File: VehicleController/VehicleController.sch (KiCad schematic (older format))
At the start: 58 parts, among them J1 CONN_02X06, J2 USF_SLAVE_I2C, J3 USB_A, J4 USB_A, J5 I2C_0, J6 I2C_1, P1 OUTPUTS, P2 OUTPUTS, Q1 Shutdown_FET, Q2 AIR_FET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

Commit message: Re-do MX120, GDS->GSD, Associations.
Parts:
- removed Q1: Shutdown_FET, TO_SOT_Packages_SMD:SOT-23_Handsoldering, symbol Q_NMOS_GDS
- removed Q2: AIR_FET, TO_SOT_Packages_SMD:SOT-23_Handsoldering, symbol Q_NMOS_GDS
- added Q1, Q2: Q_NMOS_GSD, TO_SOT_Packages_SMD:SOT-23_Handsoldering, symbol Q_NMOS_GSD
- BT1: footprint (none) -> UNCA Motorsports:BATT_CR1220
- D1, D2: footprint (none) -> Diodes_SMD:D_SOD-323_HandSoldering
- F1, F2, F3, F4, F5, F6, F7, F8: footprint (none) -> Resistors_SMD:R_1210_HandSoldering
- J1, P1, P2: footprint (none) -> UNCA Motorsports:MX120G-12
- J2, J5, J6: footprint (none) -> Pin_Headers:Pin_Header_Straight_1x03_Pitch2.54mm
- U1, U2: footprint (none) -> UNCA Motorsports:SOIC20-WIDE
- U3: footprint UNCAMotorsports:TO-252-5 -> UNCA Motorsports:TO-252-5
- U4: footprint (none) -> UNCA Motorsports:TO-252-5
- U5: footprint UNCAMotorsports:LGA-16-3x3 -> UNCA Motorsports:LGA-16-3x3
- U6: footprint UNCAMotorsports:UltimateSensorFusion -> UNCA Motorsports:UltimateSensorFusion
- U7: footprint UNCAMotorsports:Teensy_3.5 -> UNCA Motorsports:Teensy_3.5

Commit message: Library Fixes
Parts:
- BT1: footprint UNCA Motorsports:BATT_CR1220 -> UNCAMotorsports:BATT_CR1220
- D1, D2: footprint Diodes_SMD:D_SOD-323_HandSoldering -> Diodes_SMD:SOD-323
- J1, P1, P2: footprint UNCA Motorsports:MX120G-12 -> UNCAMotorsports:MX120G-12
- J2, J5, J6: footprint Pin_Headers:Pin_Header_Straight_1x03_Pitch2.54mm -> Pin_Headers:Pin_Header_Straight_1x03
- U1, U2: footprint UNCA Motorsports:SOIC20-WIDE -> UNCAMotorsports:SOIC20-WIDE
- U3, U4: footprint UNCA Motorsports:TO-252-5 -> UNCAMotorsports:TO-252-5
- U5: footprint UNCA Motorsports:LGA-16-3x3 -> UNCAMotorsports:LGA-16-3x3
- U6: footprint UNCA Motorsports:UltimateSensorFusion -> UNCAMotorsports:UltimateSensorFusion
- U7: footprint UNCA Motorsports:Teensy_3.5 -> UNCAMotorsports:Teensy_3.5
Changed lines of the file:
@@
 F 0 "BT1" H 6718 3846 50  0000 L CNN
 F 1 "CR1220" H 6718 3755 50  0000 L CNN
-F 2 "UNCA Motorsports:BATT_CR1220" V 6600 3810 50  0001 C CNN
+F 2 "UNCAMotorsports:BATT_CR1220" V 6600 3810 50  0001 C CNN
 F 3 "" V 6600 3810 50  0000 C CNN
 	1    6600 3750
@@
 F 0 "U6" H 10450 9437 60  0000 C CNN
 F 1 "UltimateSensorFusion" H 10450 9331 60  0000 C CNN
-F 2 "UNCA Motorsports:UltimateSensorFusion" H 10450 8850 60  0001 C CNN
+F 2 "UNCAMotorsports:UltimateSensorFusion" H 10450 8850 60  0001 C CNN
 F 3 "" H 10450 8850 60  0001 C CNN
 	1    10450 8950
@@
 F 0 "U3" H 3150 3437 60  0000 C CNN
 F 1 "BTS6133D" H 3150 3331 60  0000 C CNN
-F 2 "UNCA Motorsports:TO-252-5" H 3300 3250 60  0001 C CNN
+F 2 "UNCAMotorsports:TO-252-5" H 3300 3250 60  0001 C CNN
 F 3 "" H 3300 3250 60  0000 C CNN
 	1    3150 3050
@@
 F 0 "U5" H 8700 10037 60  0000 C CNN
 F 1 "H3LIS331DL" H 8700 9931 60  0000 C CNN
-F 2 "UNCA Motorsports:LGA-16-3x3" H 8500 9350 60  0001 C CNN
+F 2 "UNCAMotorsports:LGA-16-3x3" H 8500 9350 60  0001 C CNN
 F 3 "" H 8500 9350 60  0000 C CNN
 	1    8700 9250
@@
 F 0 "U4" H 2950 5200 60  0000 C CNN
 F 1 "BTS6133D" H 3200 4700 60  0000 C CNN
-F 2 "UNCA Motorsports:TO-252-5" H 3300 5150 60  0001 C CNN
+F 2 "UNCAMotorsports:TO-252-5" H 3300 5150 60  0001 C CNN
 F 3 "" H 3300 5150 60  0000 C CNN
 	1    3150 4950
@@
 F 0 "U7" H 10650 5387 60  0000 C CNN
 F 1 "Teensy_3.5" H 10650 5281 60  0000 C CNN
-F 2 "UNCA Motorsports:Teensy_3.5" H 11100 4650 60  0001 C CNN
+F 2 "UNCAMotorsports:Teensy_3.5" H 11100 4650 60  0001 C CNN
 F 3 "" H 11100 4650 60  0000 C CNN
 	1    10650 3950
@@
 F 0 "U1" H 1800 7500 60  0000 C CNN
 F 1 "BTS4130QGA" H 2050 6300 60  0000 C CNN
-F 2 "UNCA Motorsports:SOIC20-WIDE" H 2100 7100 60  0001 C CNN
+F 2 "UNCAMotorsports:SOIC20-WIDE" H 2100 7100 60  0001 C CNN
 F 3 "" H 2100 7100 60  0001 C CNN
 	1    2100 7100
@@
 F 0 "P2" H 3350 9750 50  0000 C CNN
 F 1 "OUTPUTS" H 3350 9250 50  0000 C CNN
-F 2 "UNCA Motorsports:MX120G-12" H 3350 8300 50  0001 C CNN
+F 2 "UNCAMotorsports:MX120G-12" H 3350 8300 50  0001 C CNN
 F 3 "" H 3350 8300 50  0000 C CNN
 	1    3350 9500
@@
 F 0 "U2" H 1800 9400 60  0000 C CNN
 F 1 "BTS4130QGA" H 2050 8200 60  0000 C CNN
-F 2 "UNCA Motorsports:SOIC20-WIDE" H 2100 9000 60  0001 C CNN
+F 2 "UNCAMotorsports:SOIC20-WIDE" H 2100 9000 60  0001 C CNN
 F 3 "" H 2100 9000 60  0001 C CNN
 	1    2100 9000
@@
 F 0 "P1" H 3350 7850 50  0000 C CNN
 F 1 "OUTPUTS" H 3350 7350 50  0000 C CNN
-F 2 "UNCA Motorsports:MX120G-12" H 3350 6400 50  0001 C CNN
+F 2 "UNCAMotorsports:MX120G-12" H 3350 6400 50  0001 C CNN
 F 3 "" H 3350 6400 50  0000 C CNN
 	1    3350 7600
@@
 F 0 "D1" H 2400 3440 50  0000 C CNN
 F 1 "3.3V" H 2400 3260 50  0000 C CNN
-F 2 "Diodes_SMD:D_SOD-323_HandSoldering" V 2400 3350 50  0001 C CNN
+F 2 "Diodes_SMD:SOD-323" V 2400 3350 50  0001 C CNN
 F 3 "" V 2400 3350 50  0001 C CNN
 	1    2400 3350
@@
 F 0 "D2" H 9100 5590 50  0000 C CNN
 F 1 "3.3V" H 9100 5410 50  0000 C CNN
-F 2 "Diodes_SMD:D_SOD-323_HandSoldering" V 9100 5500 50  0001 C CNN
+F 2 "Diodes_SMD:SOD-323" V 9100 5500 50  0001 C CNN
 F 3 "" V 9100 5500 50  0001 C CNN
 	1    9100 5500
@@
 F 0 "J5" H 14600 6800 50  0000 C CNN
 F 1 "I2C_0" V 14700 6600 50  0000 C CNN
-F 2 "Pin_Headers:Pin_Header_Straight_1x03_Pitch2.54mm" H 14600 6600 50  0001 C CNN
+F 2 "Pin_Headers:Pin_Header_Straight_1x03" H 14600 6600 50  0001 C CNN
 F 3 "" H 14600 6600 50  0001 C CNN
 	1    14600 6600
@@
 F 0 "J6" H 14600 7700 50  0000 C CNN
 F 1 "I2C_1" V 14700 7500 50  0000 C CNN
-F 2 "Pin_Headers:Pin_Header_Straight_1x03_Pitch2.54mm" H 14600 7500 50  0001 C CNN
+F 2 "Pin_Headers:Pin_Header_Straight_1x03" H 14600 7500 50  0001 C CNN
 F 3 "" H 14600 7500 50  0001 C CNN
 	1    14600 7500
@@
 F 0 "J2" H 9000 8300 50  0000 C CNN
 F 1 "USF_SLAVE_I2C" V 9100 8100 50  0000 C CNN
-F 2 "Pin_Headers:Pin_Header_Straight_1x03_Pitch2.54mm" H 9000 8100 50  0001 C CNN
+F 2 "Pin_Headers:Pin_Header_Straight_1x03" H 9000 8100 50  0001 C CNN
 F 3 "" H 9000 8100 50  0001 C CNN
 	1    9000 8100
@@
 F 0 "J1" H 1600 2550 50  0000 C CNN
 F 1 "CONN_02X06" H 1600 1850 50  0000 C CNN
-F 2 "UNCA Motorsports:MX120G-12" H 1600 1000 50  0001 C CNN
+F 2 "UNCAMotorsports:MX120G-12" H 1600 1000 50  0001 C CNN
 F 3 "" H 1600 1000 50  0001 C CNN
 	1    1600 2200

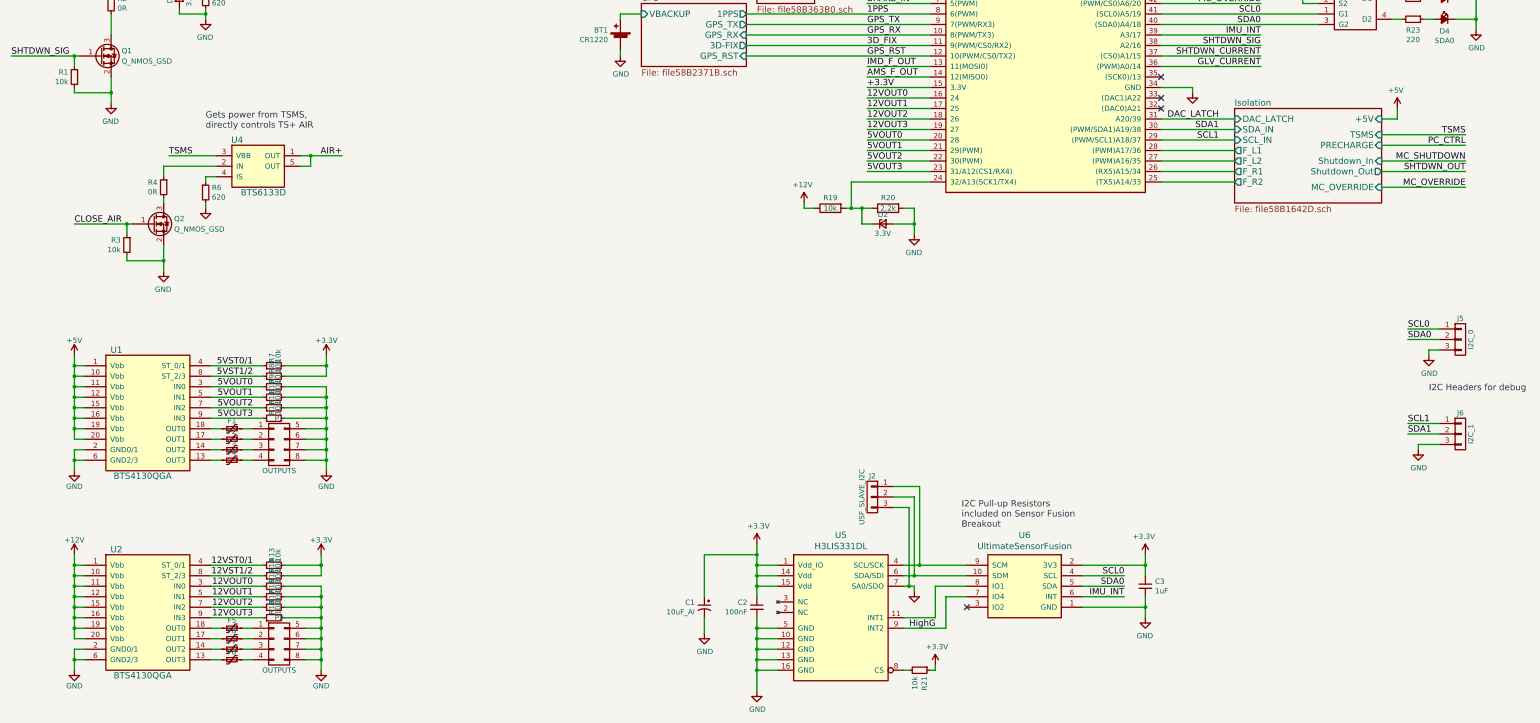
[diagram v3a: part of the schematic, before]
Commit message: Major layout of VCU begins.  Moved some nets to facilitate layout
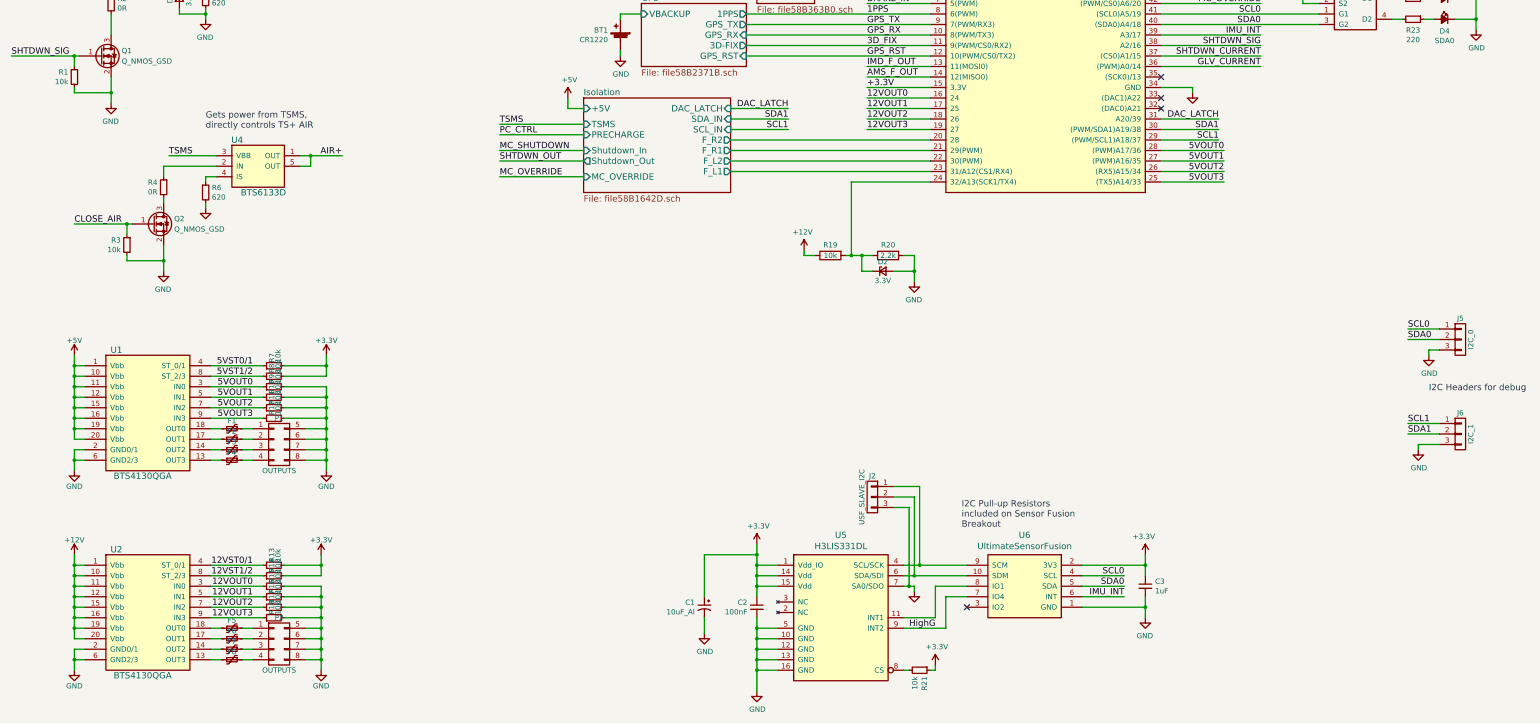
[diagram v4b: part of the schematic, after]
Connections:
- net 5VOUT0: now also U7.28 ((PWM)A17/36); no longer U7.20 (28)
- net 5VOUT1: now also U7.27 ((PWM)A16/35); no longer U7.21 (29(PWM))
- net 5VOUT2: now also U7.26 ((RX5)A15/34); no longer U7.22 (30(PWM))
- net 5VOUT3: now also U7.25 ((TX5)A14/33); no longer U7.23 (31/A12(CS1/RX4))
- net Isolation/F_L1: now also U7.23 (31/A12(CS1/RX4)); no longer U7.28 ((PWM)A17/36)
- net Isolation/F_L2: now also U7.22 (30(PWM)); no longer U7.27 ((PWM)A16/35)
- net Isolation/F_R1: now also U7.21 (29(PWM)); no longer U7.26 ((RX5)A15/34)
- net Isolation/F_R2: now also U7.20 (28); no longer U7.25 ((TX5)A14/33)
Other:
- moved on the sheet: D2, R19, R20

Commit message: More VCU layout work
connectors changed to 2x4 molex nanofits for the 12v and 5v outputs.
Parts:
- P1, P2: footprint UNCAMotorsports:MX120G-12 -> Connectors_Molex:Molex_NanoFit_2x04x2.50mm_Straight
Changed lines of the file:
@@
 F 0 "P2" H 3350 9750 50  0000 C CNN
 F 1 "OUTPUTS" H 3350 9250 50  0000 C CNN
-F 2 "UNCAMotorsports:MX120G-12" H 3350 8300 50  0001 C CNN
+F 2 "Connectors_Molex:Molex_NanoFit_2x04x2.50mm_Straight" H 3350 8300 50  0001 C CNN
 F 3 "" H 3350 8300 50  0000 C CNN
 	1    3350 9500
@@
 F 0 "P1" H 3350 7850 50  0000 C CNN
 F 1 "OUTPUTS" H 3350 7350 50  0000 C CNN
-F 2 "UNCAMotorsports:MX120G-12" H 3350 6400 50  0001 C CNN
+F 2 "Connectors_Molex:Molex_NanoFit_2x04x2.50mm_Straight" H 3350 6400 50  0001 C CNN
 F 3 "" H 3350 6400 50  0000 C CNN
 	1    3350 7600

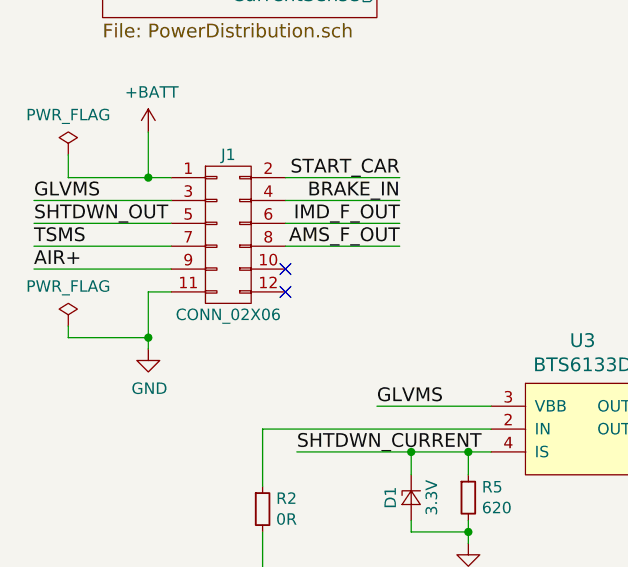
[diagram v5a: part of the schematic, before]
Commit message: 2x10 connector is now a nanofit, VCU
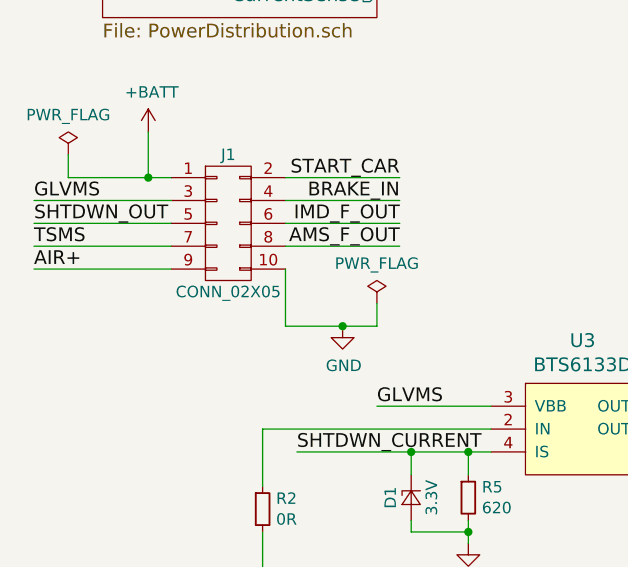
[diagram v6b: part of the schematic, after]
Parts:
- removed J1: CONN_02X06, UNCAMotorsports:MX120G-12, symbol CONN_02X06
- added J1: CONN_02X05, Connectors_Molex:Molex_NanoFit_2x05x2.50mm_Straight, symbol CONN_02X05
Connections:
- net +BATT: now also J1.1 (P1)
- net AIR+: now also J1.9 (P9)
- net AMS_F_OUT: now also J1.8 (P8)
- net BRAKE_IN: now also J1.4 (P4)
- net GLVMS: now also J1.3 (P3)
- net GND: now also J1.10 (P10)
- net IMD_F_OUT: now also J1.6 (P6)
- net SHTDWN_OUT: now also J1.5 (P5)
- net START_CAR: now also J1.2 (P2)
- net TSMS: now also J1.7 (P7)
- no-connect marks 10 -> 8
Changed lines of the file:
@@
 L GND #PWR016
 U 1 1 58BAD6C3
-P 1250 2700
-F 0 "#PWR016" H 1250 2450 50  0001 C CNN
-F 1 "GND" H 1255 2527 50  0000 C CNN
-F 2 "" H 1250 2700 50  0000 C CNN
-F 3 "" H 1250 2700 50  0000 C CNN
-	1    1250 2700
+P 2100 2600
+F 0 "#PWR016" H 2100 2350 50  0001 C CNN
+F 1 "GND" H 2105 2427 50  0000 C CNN
+F 2 "" H 2100 2600 50  0000 C CNN
+F 3 "" H 2100 2600 50  0000 C CNN
+	1    2100 2600
 	1    0    0    -1
 $EndComp
@@
 L PWR_FLAG #FLG022
 U 1 1 58BF6049
-P 900 2600
-F 0 "#FLG022" H 350 1825 50  0001 C CNN
-F 1 "PWR_FLAG" H 900 2774 50  0000 C CNN
-F 2 "" H 350 1750 50  0001 C CNN
-F 3 "" H 350 1750 50  0001 C CNN
-	1    900  2600
+P 2250 2500
+F 0 "#FLG022" H 1700 1725 50  0001 C CNN
+F 1 "PWR_FLAG" H 2250 2674 50  0000 C CNN
+F 2 "" H 1700 1650 50  0001 C CNN
+F 3 "" H 1700 1650 50  0001 C CNN
+	1    2250 2500
 	1    0    0    -1
 $EndComp
@@
 	-1   0    0    -1
 $EndComp
-$Comp
-L CONN_02X06 J1
-U 1 1 58F667AB
-P 1600 2200
-F 0 "J1" H 1600 2550 50  0000 C CNN
-F 1 "CONN_02X06" H 1600 1850 50  0000 C CNN
-F 2 "UNCAMotorsports:MX120G-12" H 1600 1000 50  0001 C CNN
-F 3 "" H 1600 1000 50  0001 C CNN
-	1    1600 2200
-	1    0    0    -1
-$EndComp
 Connection ~ 9400 8850
 Wire Wire Line
@@
 Wire Wire Line
 	1750 3500 1750 3700
-Connection ~ 1250 2650
-Wire Wire Line
-	900  2650 1250 2650
-Wire Wire Line
-	900  2600 900  2650
 Connection ~ 1250 1950
 Wire Wire Line
@@
 Wire Wire Line
 	850  950  850  850
-Wire Wire Line
-	1250 2450 1350 2450
-Wire Wire Line
-	1250 2450 1250 2700
 Wire Wire Line
 	900  1950 1350 1950
@@
 Wire Wire Line
 	2750 1050 2750 850
-NoConn ~ 1850 2350
-NoConn ~ 1850 2450
 $Comp
 L Q_NMOS_GSD Q1
@@
 Wire Wire Line
 	7650 4600 8200 4600
+$Comp
+L CONN_02X05 J1
+U 1 1 59308E1C
+P 1600 2150
+F 0 "J1" H 1600 2450 50  0000 C CNN
+F 1 "CONN_02X05" H 1600 1850 50  0000 C CNN
+F 2 "Connectors_Molex:Molex_NanoFit_2x05x2.50mm_Straight" H 1600 950 50  0001 C CNN
+F 3 "" H 1600 950 50  0001 C CNN
+	1    1600 2150
+	1    0    0    -1
+$EndComp
+Wire Wire Line
+	1850 2350 1850 2600
+Wire Wire Line
+	1850 2600 2250 2600
+Wire Wire Line
+	2250 2600 2250 2500
+Connection ~ 2100 2600
 $EndSCHEMATC

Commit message: Major VCU Layout changes
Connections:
- net 12VOUT0: now also U7.19 (27); no longer U7.16 (24)
- net 12VOUT1: now also U7.18 (26); no longer U7.17 (25)
- net 12VOUT2: now also U7.17 (25); no longer U7.18 (26)
- net 12VOUT3: now also U7.16 (24); no longer U7.19 (27)
- net 5VOUT0: now also U7.23 (31/A12(CS1/RX4)); no longer U7.28 ((PWM)A17/36)
- net 5VOUT1: now also U7.22 (30(PWM)); no longer U7.27 ((PWM)A16/35)
- net 5VOUT2: now also U7.21 (29(PWM)); no longer U7.26 ((RX5)A15/34)
- net 5VOUT3: now also U7.20 (28); no longer U7.25 ((TX5)A14/33)
- net AIR+: now also J1.8 (P8); no longer J1.9 (P9)
- net AMS_F_OUT: now also J1.10 (P10); no longer J1.8 (P8)
- net BRAKE_IN: now also J1.7 (P7); no longer J1.4 (P4)
- net CLOSE_AIR: now also U7.24 (32/A13(SCK1/TX4)); no longer U7.3 (1(MISO1/TX1))
- net GND: now also J1.5 (P5), P1.1 (P1), P1.2 (P3), P1.3 (P5), P1.4 (P7), P2.1 (P1), P2.2 (P3), P2.3 (P5), P2.4 (P7); no longer J1.10 (P10), P1.5 (P2), P1.6 (P4), P1.7 (P6), P1.8 (P8), P2.5 (P2), P2.6 (P4), P2.7 (P6), P2.8 (P8)
- net IMD_F_OUT: now also J1.9 (P9); no longer J1.6 (P6)
- net IMU_INT: now also U7.27 ((PWM)A16/35); no longer U7.39 (A3/17)
- net Isolation/F_L1: no longer U7.23 (31/A12(CS1/RX4))
- net Isolation/F_L2: no longer U7.22 (30(PWM))
- net Isolation/F_R1: no longer U7.21 (29(PWM))
- net Isolation/F_R2: no longer U7.20 (28)
- net MC_OVERRIDE: now also U7.26 ((RX5)A15/34); no longer U7.42 ((PWM/CS0)A6/20)
- net PC_CTRL: now also U7.25 ((TX5)A14/33); no longer U7.4 (2(PWM))
- net SHTDWN_CURRENT: now also U7.33 ((DAC1)A22); no longer U7.37 ((CS0)A1/15)
- net SHTDWN_OUT: now also J1.4 (P4); no longer J1.5 (P5)
- net SHTDWN_SIG: now also U7.28 ((PWM)A17/36); no longer U7.38 (A2/16)
- net START_CAR: now also J1.6 (P6); no longer J1.2 (P2)
- net TSMS: now also J1.2 (P2); no longer J1.7 (P7)
- net BATT_SENSE: now reaches D2.1 (K), R19.2, R20.1
- net BATT_SENSE: now also U7.32 ((DAC0)A21); no longer U7.24 (32/A13(SCK1/TX4))
- net at F1.1: now also P1.8 (P8); no longer P1.1 (P1)
- net at F2.1: now also P1.7 (P6); no longer P1.2 (P3)
- net at F3.1: now also P1.6 (P4); no longer P1.3 (P5)
- net at F4.1: now also P1.5 (P2); no longer P1.4 (P7)
- net at F5.1: now also P2.8 (P8); no longer P2.1 (P1)
- net at F6.1: now also P2.7 (P6); no longer P2.2 (P3)
- net at F7.1: now also P2.6 (P4); no longer P2.3 (P5)
- net at F8.1: now also P2.5 (P2); no longer P2.4 (P7)
- no-connect marks 8 -> 7
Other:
- moved on the sheet: D2, R19, R20
